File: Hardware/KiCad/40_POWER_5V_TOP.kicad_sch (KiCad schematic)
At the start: 0 parts

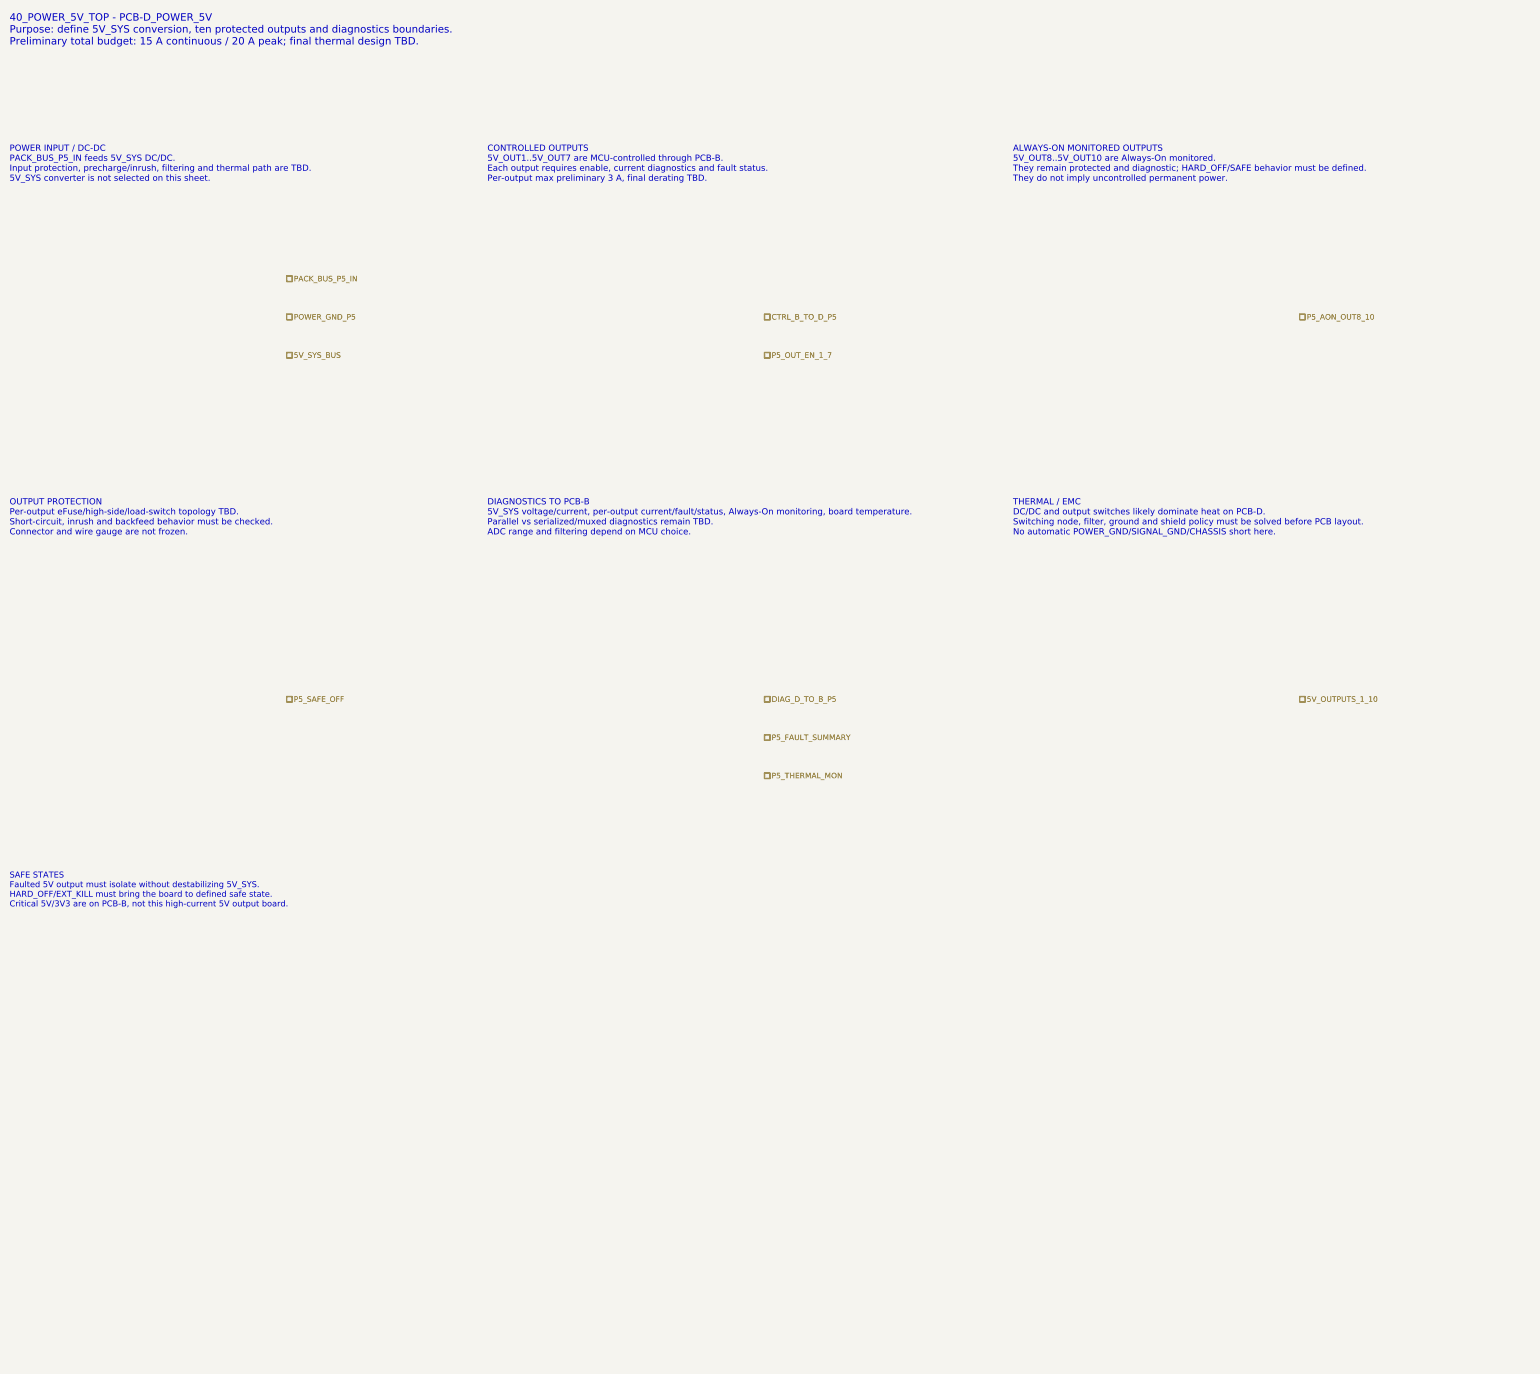
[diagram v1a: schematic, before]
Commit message: hardware: add PCB-D POWER_5V detailed hierarchy
Merge PCB-D Architecture Level A/B hierarchy after preserving conversion, output, diagnostic, and safe-state boundaries.
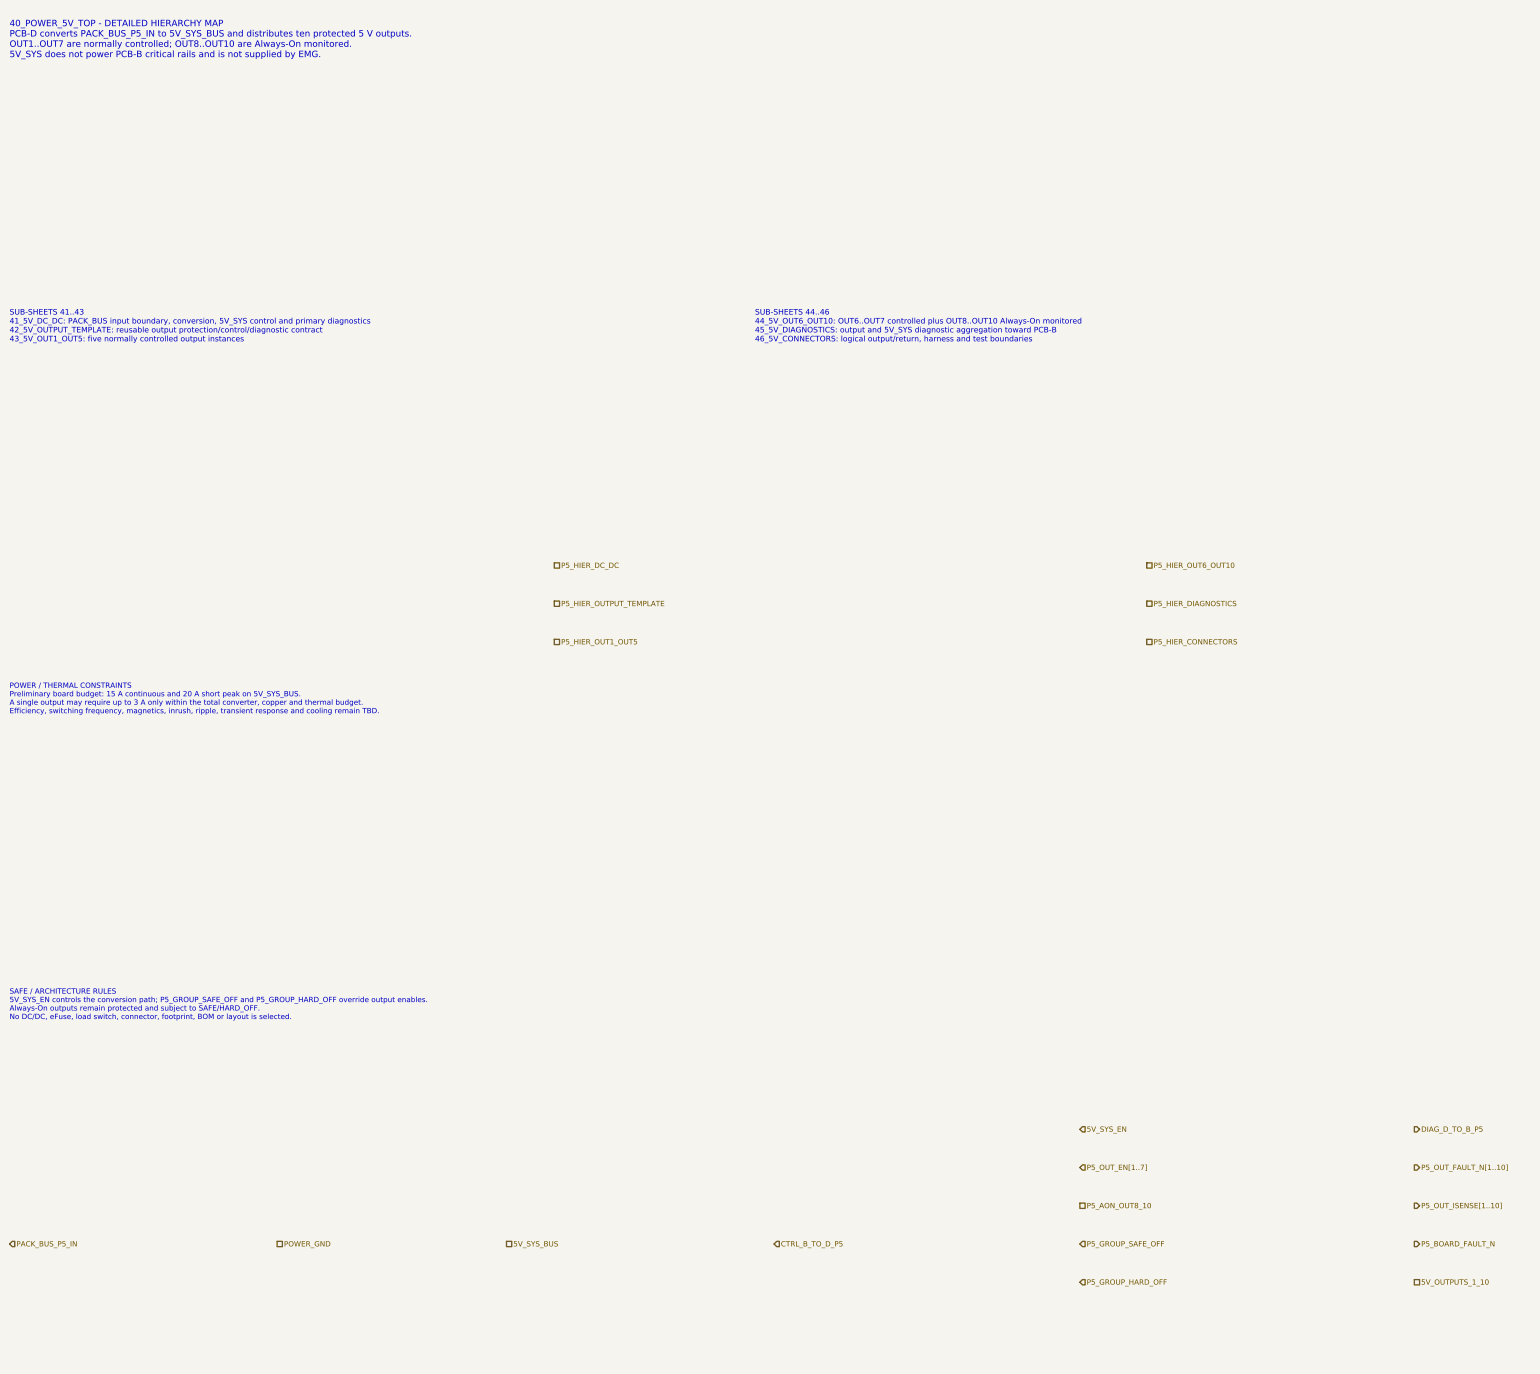
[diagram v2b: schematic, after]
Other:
- note added: "40_POWER_5V_TOP - DETAILED HIERARCHY MAP PCB-D converts PACK_BUS_P5_IN to 5V_SYS_BUS and distributes ten protected 5 V outputs. OUT1..OUT7 are normally controlled; OUT8..OUT10 are Always-On monitored. 5V_SYS does not power PCB-B critical rails and is not supplied by EMG."
- note added: "POWER / THERMAL CONSTRAINTS Preliminary board budget: 15 A continuous and 20 A short peak on 5V_SYS_BUS. A single output may require up to 3 A only within the total converter, copper and thermal budget. Efficiency, switching frequency, magnetics, inrush, ripple, transient response and cooling remain TBD."
- note added: "SAFE / ARCHITECTURE RULES 5V_SYS_EN controls the conversion path; P5_GROUP_SAFE_OFF and P5_GROUP_HARD_OFF override output enables. Always-On outputs remain protected and subject to SAFE/HARD_OFF. No DC/DC, eFuse, load switch, connector, footprint, BOM or layout is selected."
- note added: "SUB-SHEETS 41..43 41_5V_DC_DC: PACK_BUS input boundary, conversion, 5V_SYS control and primary diagnostics 42_5V_OUTPUT_TEMPLATE: reusable output protection/control/diagnostic contract 43_5V_OUT1_OUT5: five normally controlled output instances"
- note added: "SUB-SHEETS 44..46 44_5V_OUT6_OUT10: OUT6..OUT7 controlled plus OUT8..OUT10 Always-On monitored 45_5V_DIAGNOSTICS: output and 5V_SYS diagnostic aggregation toward PCB-B 46_5V_CONNECTORS: logical output/return, harness and test boundaries"
- note removed: "40_POWER_5V_TOP - PCB-D_POWER_5V Purpose: define 5V_SYS conversion, ten protected outputs and diagnostics boundaries. Preliminary total budget: 15 A continuous / 20 A peak; final thermal design TBD."
- note removed: "ALWAYS-ON MONITORED OUTPUTS 5V_OUT8..5V_OUT10 are Always-On monitored. They remain protected and diagnostic; HARD_OFF/SAFE behavior must be defined. They do not imply uncontrolled permanent power."
- note removed: "CONTROLLED OUTPUTS 5V_OUT1..5V_OUT7 are MCU-controlled through PCB-B. Each output requires enable, current diagnostics and fault status. Per-output max preliminary 3 A, final derating TBD."
- note removed: "DIAGNOSTICS TO PCB-B 5V_SYS voltage/current, per-output current/fault/status, Always-On monitoring, board temperature. Parallel vs serialized/muxed diagnostics remain TBD. ADC range and filtering depend on MCU choice."
- note removed: "OUTPUT PROTECTION Per-output eFuse/high-side/load-switch topology TBD. Short-circuit, inrush and backfeed behavior must be checked. Connector and wire gauge are not frozen."
- note removed: "POWER INPUT / DC-DC PACK_BUS_P5_IN feeds 5V_SYS DC/DC. Input protection, precharge/inrush, filtering and thermal path are TBD. 5V_SYS converter is not selected on this sheet."
- note removed: "SAFE STATES Faulted 5V output must isolate without destabilizing 5V_SYS. HARD_OFF/EXT_KILL must bring the board to defined safe state. Critical 5V/3V3 are on PCB-B, not this high-current 5V output board."
- note removed: "THERMAL / EMC DC/DC and output switches likely dominate heat on PCB-D. Switching node, filter, ground and shield policy must be solved before PCB layout. No automatic POWER_GND/SIGNAL_GND/CHASSIS short here."

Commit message: hardware: align PCB-D top boundary to local CAN-FD control
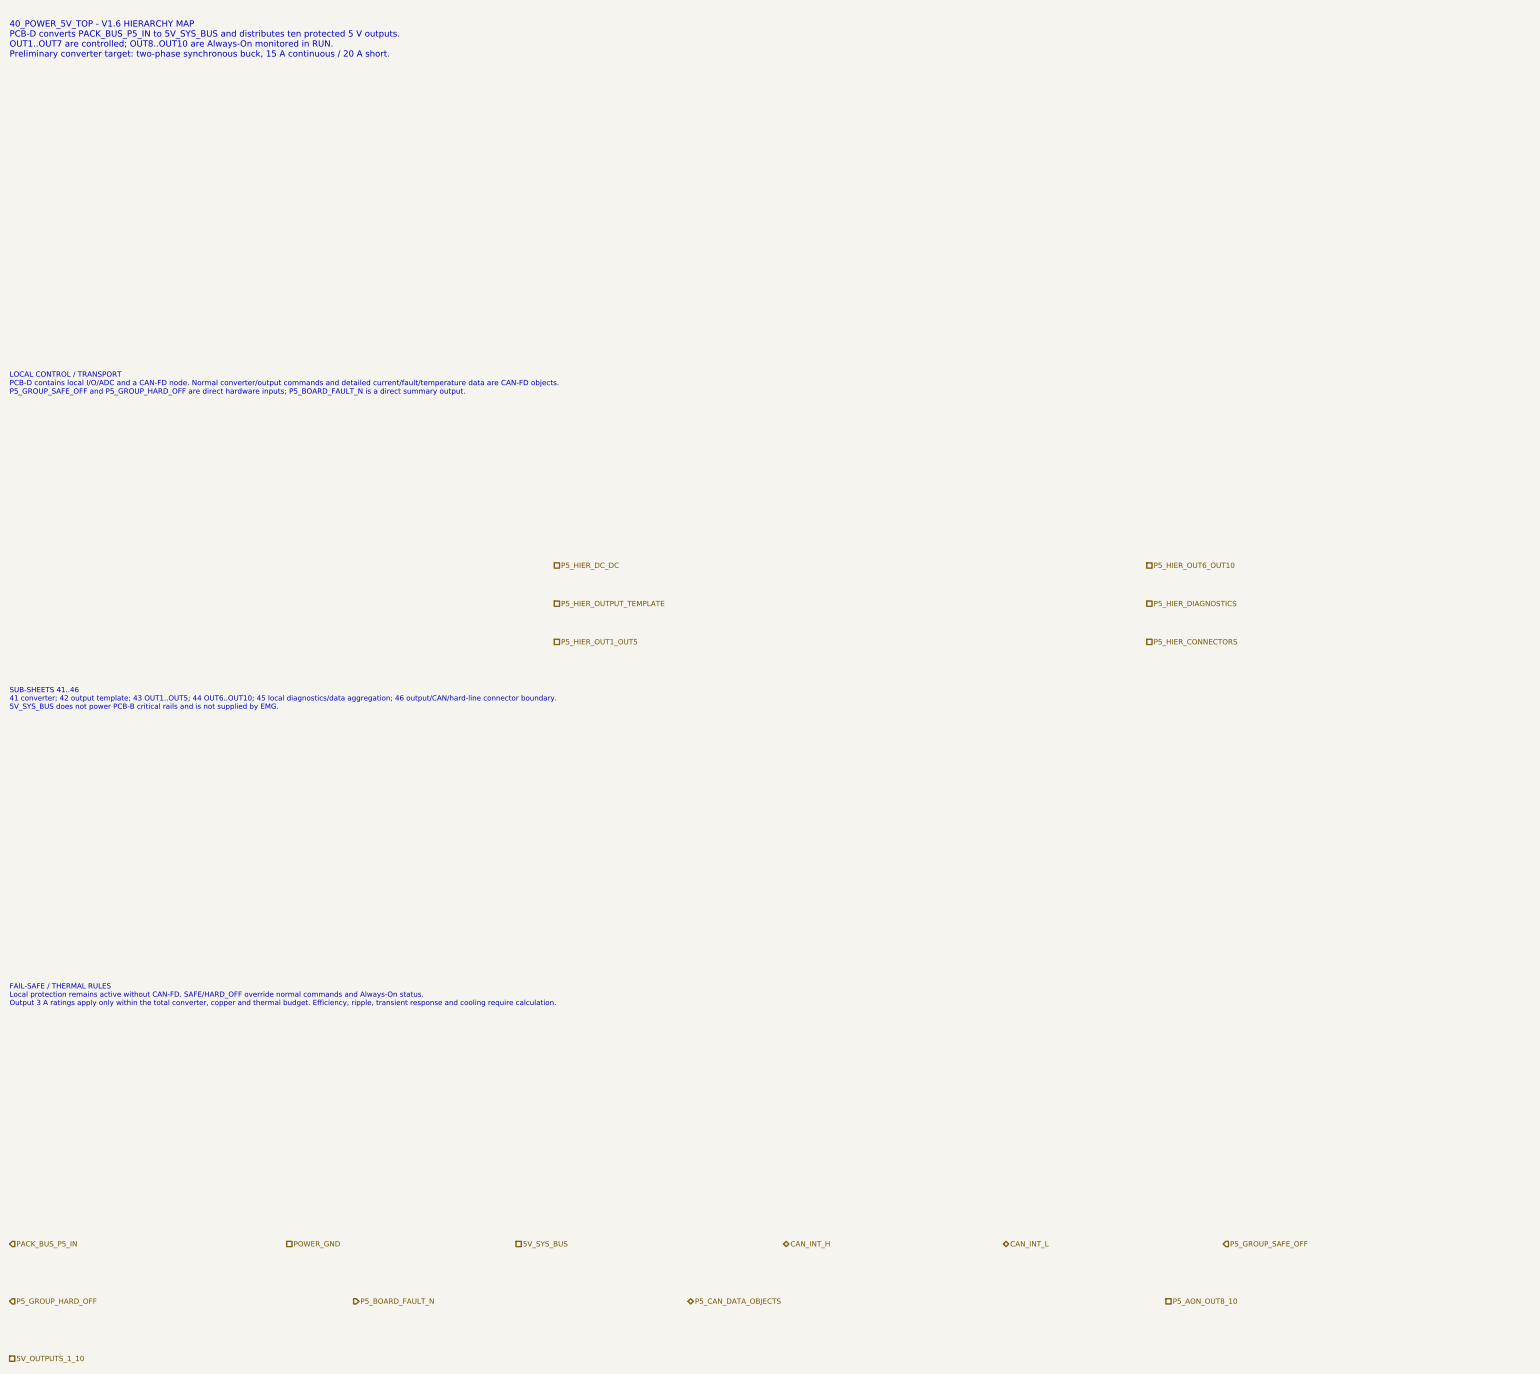
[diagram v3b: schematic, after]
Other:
- note added: "40_POWER_5V_TOP - V1.6 HIERARCHY MAP PCB-D converts PACK_BUS_P5_IN to 5V_SYS_BUS and distributes ten protected 5 V outputs. OUT1..OUT7 are controlled; OUT8..OUT10 are Always-On monitored in RUN. Preliminary converter target: two-phase synchronous buck, 15 A continuous / 20 A short."
- note added: "FAIL-SAFE / THERMAL RULES Local protection remains active without CAN-FD. SAFE/HARD_OFF override normal commands and Always-On status. Output 3 A ratings apply only within the total converter, copper and thermal budget. Efficiency, ripple, transient response and cooling require calculation."
- note added: "LOCAL CONTROL / TRANSPORT PCB-D contains local I/O/ADC and a CAN-FD node. Normal converter/output commands and detailed current/fault/temperature data are CAN-FD objects. P5_GROUP_SAFE_OFF and P5_GROUP_HARD_OFF are direct hardware inputs; P5_BOARD_FAULT_N is a direct summary output."
- note added: "SUB-SHEETS 41..46 41 converter; 42 output template; 43 OUT1..OUT5; 44 OUT6..OUT10; 45 local diagnostics/data aggregation; 46 output/CAN/hard-line connector boundary. 5V_SYS_BUS does not power PCB-B critical rails and is not supplied by EMG."
- note removed: "40_POWER_5V_TOP - DETAILED HIERARCHY MAP PCB-D converts PACK_BUS_P5_IN to 5V_SYS_BUS and distributes ten protected 5 V outputs. OUT1..OUT7 are normally controlled; OUT8..OUT10 are Always-On monitored. 5V_SYS does not power PCB-B critical rails and is not supplied by EMG."
- note removed: "POWER / THERMAL CONSTRAINTS Preliminary board budget: 15 A continuous and 20 A short peak on 5V_SYS_BUS. A single output may require up to 3 A only within the total converter, copper and thermal budget. Efficiency, switching frequency, magnetics, inrush, ripple, transient response and cooling remain TBD."
- note removed: "SAFE / ARCHITECTURE RULES 5V_SYS_EN controls the conversion path; P5_GROUP_SAFE_OFF and P5_GROUP_HARD_OFF override output enables. Always-On outputs remain protected and subject to SAFE/HARD_OFF. No DC/DC, eFuse, load switch, connector, footprint, BOM or layout is selected."
- note removed: "SUB-SHEETS 41..43 41_5V_DC_DC: PACK_BUS input boundary, conversion, 5V_SYS control and primary diagnostics 42_5V_OUTPUT_TEMPLATE: reusable output protection/control/diagnostic contract 43_5V_OUT1_OUT5: five normally controlled output instances"
- note removed: "SUB-SHEETS 44..46 44_5V_OUT6_OUT10: OUT6..OUT7 controlled plus OUT8..OUT10 Always-On monitored 45_5V_DIAGNOSTICS: output and 5V_SYS diagnostic aggregation toward PCB-B 46_5V_CONNECTORS: logical output/return, harness and test boundaries"
